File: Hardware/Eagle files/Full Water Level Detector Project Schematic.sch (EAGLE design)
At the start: 20 parts, among them IC1 74AHCT125, M1 SMALL_SERVO

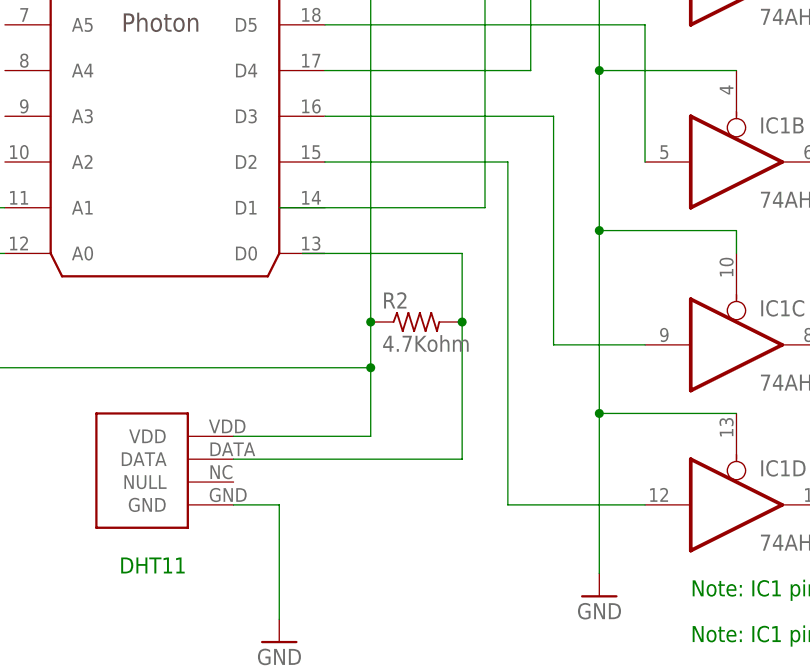
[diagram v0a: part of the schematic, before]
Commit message: Updated schematic
Changed DHT11 data to Photon D2 instead of D0.  D0 does not work with
Piettetech library.  Changed IC1D input to D0 to free up D2 for the
DHT11.
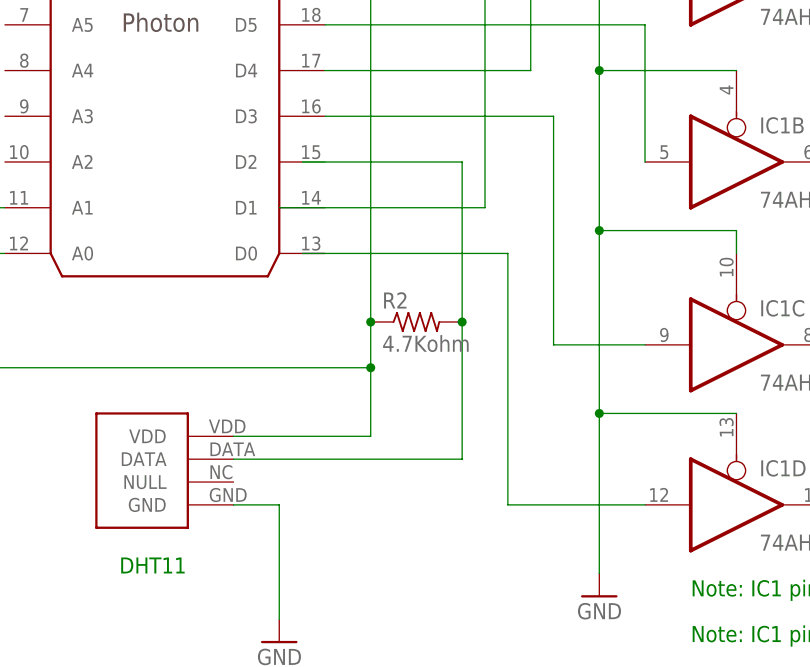
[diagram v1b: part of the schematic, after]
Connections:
- net N$17: no longer U$1G$1.D2
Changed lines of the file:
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@@
 <net name="N$17" class="0">
 <segment>
-<pinref part="U$1" gate="G$1" pin="D2"/>
-<wire x1="10.16" y1="48.26" x2="30.48" y2="48.26" width="0.1524" layer="91"/>
-<wire x1="30.48" y1="48.26" x2="30.48" y2="10.16" width="0.1524" layer="91"/>
 <pinref part="IC1" gate="D" pin="I"/>
 <wire x1="30.48" y1="10.16" x2="45.72" y2="10.16" width="0.1524" layer="91"/>
+<wire x1="7.62" y1="38.1" x2="30.48" y2="38.1" width="0.1524" layer="91"/>
+<wire x1="30.48" y1="38.1" x2="30.48" y2="10.16" width="0.1524" layer="91"/>
 </segment>
 </net>
@@
 <wire x1="0" y1="15.24" x2="25.4" y2="15.24" width="0.1524" layer="91"/>
 <wire x1="25.4" y1="15.24" x2="25.4" y2="30.48" width="0.1524" layer="91"/>
-<wire x1="25.4" y1="30.48" x2="25.4" y2="38.1" width="0.1524" layer="91"/>
-<wire x1="25.4" y1="38.1" x2="7.62" y2="38.1" width="0.1524" layer="91"/>
 <pinref part="R2" gate="G$1" pin="2"/>
+<wire x1="25.4" y1="30.48" x2="25.4" y2="48.26" width="0.1524" layer="91"/>
+<wire x1="25.4" y1="48.26" x2="7.62" y2="48.26" width="0.1524" layer="91"/>
 <junction x="25.4" y="30.48"/>
 </segment>

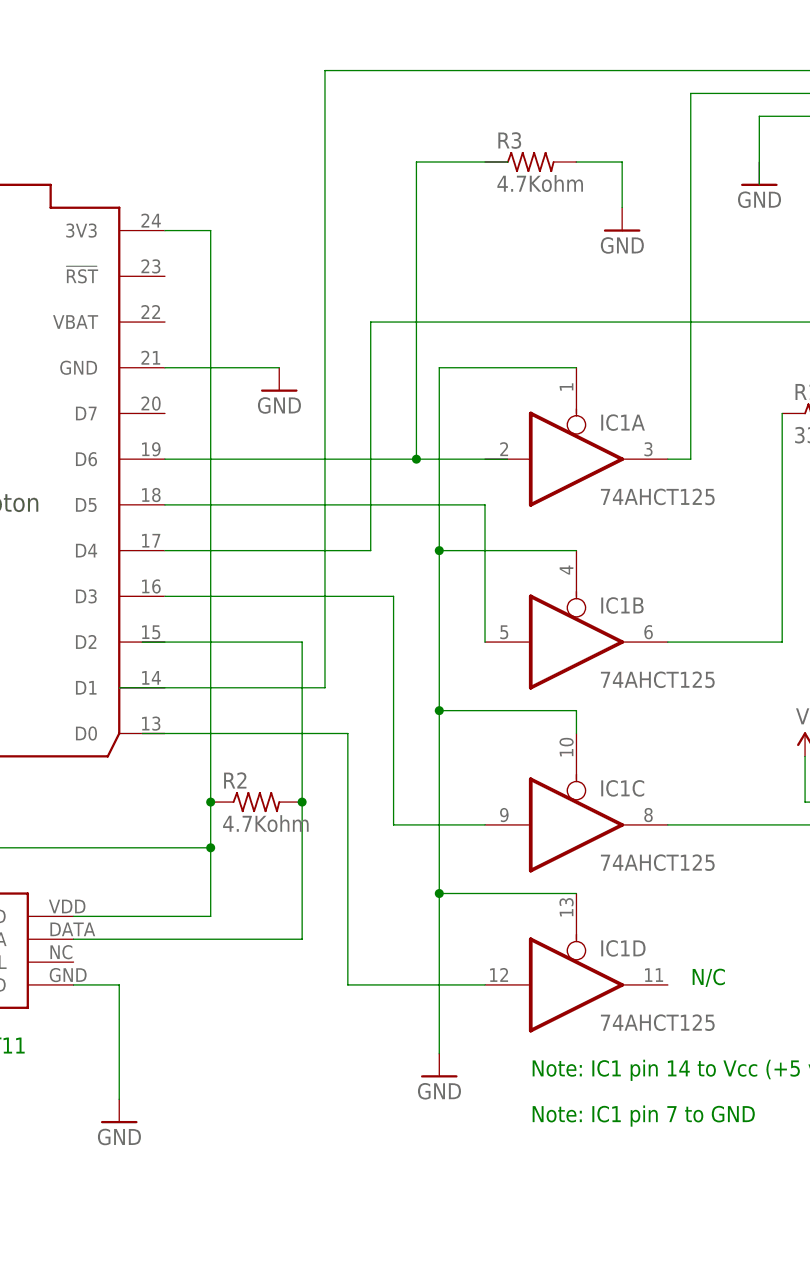
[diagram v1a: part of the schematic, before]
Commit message: Updated schematic
Placed 5.6 Kohm pulldown resistors on all input pins of the 74AHCT125 to
clamp off noise when the Photon is flashing/reset.  Used 5.6 Kohm in
lieu of 4.7 Kohm because that is what I had on hand.
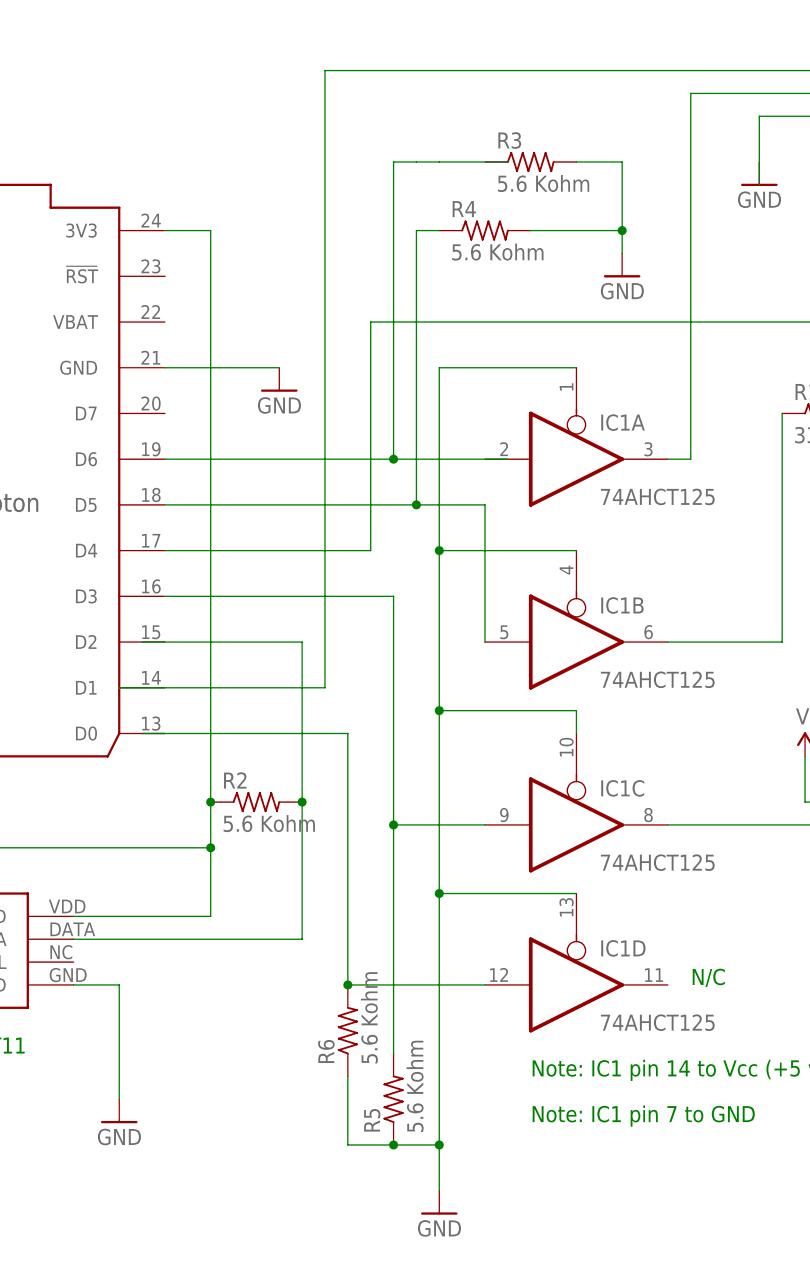
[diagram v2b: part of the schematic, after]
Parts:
- added R4, R5, R6: 5.6 Kohm, rcl:R-US_0309/12
- R2, R3: value 4.7Kohm -> 5.6 Kohm
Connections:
- net GND: now also R4.2, R5.1, R6.1
- net N$17: now also R6.2
- net N$6: now also R4.1
- net N$7: now also R5.2
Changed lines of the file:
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@@
 <part name="GND8" library="SparkFun-Aesthetics" deviceset="GND" device=""/>
 <part name="GND9" library="SparkFun-Aesthetics" deviceset="GND" device=""/>
-<part name="R2" library="rcl" deviceset="R-US_" device="0309/12" value="4.7Kohm"/>
+<part name="R2" library="rcl" deviceset="R-US_" device="0309/12" value="5.6 Kohm"/>
 <part name="TOGGLE" library="switch" deviceset="55?" device="01"/>
-<part name="R3" library="rcl" deviceset="R-US_" device="0309/12" value="4.7Kohm"/>
+<part name="R3" library="rcl" deviceset="R-US_" device="0309/12" value="5.6 Kohm"/>
 <part name="GND10" library="SparkFun-Aesthetics" deviceset="GND" device=""/>
+<part name="R4" library="rcl" deviceset="R-US_" device="0309/12" value="5.6 Kohm"/>
+<part name="R5" library="rcl" deviceset="R-US_" device="0309/12" value="5.6 Kohm"/>
+<part name="R6" library="rcl" deviceset="R-US_" device="0309/12" value="5.6 Kohm"/>
 </parts>
 <sheets>
@@
 <instance part="LED1" gate="G$1" x="119.38" y="73.66" rot="R90"/>
 <instance part="SP2" gate="G$1" x="111.76" y="104.14" rot="R270"/>
-<instance part="GND5" gate="1" x="40.64" y="0" rot="MR0"/>
+<instance part="GND5" gate="1" x="40.64" y="-15.24" rot="MR0"/>
 <instance part="U$2" gate="G$1" x="-15.24" y="7.62"/>
 <instance part="GND6" gate="1" x="5.08" y="-5.08" rot="MR0"/>
@@
 <instance part="TOGGLE" gate="G$1" x="106.68" y="129.54"/>
 <instance part="R3" gate="G$1" x="50.8" y="101.6"/>
-<instance part="GND10" gate="1" x="60.96" y="93.98" rot="MR0"/>
+<instance part="GND10" gate="1" x="60.96" y="88.9" rot="MR0"/>
+<instance part="R4" gate="G$1" x="45.72" y="93.98"/>
+<instance part="R5" gate="G$1" x="35.56" y="-2.54" rot="R90"/>
+<instance part="R6" gate="G$1" x="30.48" y="5.08" rot="R90"/>
 </instances>
 <busses>
@@
 <segment>
 <pinref part="GND5" gate="1" pin="GND"/>
-<wire x1="40.64" y1="2.54" x2="40.64" y2="20.32" width="0.1524" layer="91"/>
+<wire x1="40.64" y1="-12.7" x2="40.64" y2="-7.62" width="0.1524" layer="91"/>
 <pinref part="IC1" gate="A" pin="OE"/>
+<wire x1="40.64" y1="-7.62" x2="40.64" y2="20.32" width="0.1524" layer="91"/>
 <wire x1="40.64" y1="20.32" x2="40.64" y2="40.64" width="0.1524" layer="91"/>
 <wire x1="40.64" y1="40.64" x2="40.64" y2="58.42" width="0.1524" layer="91"/>
@@
 <junction x="40.64" y="40.64"/>
 <junction x="40.64" y="58.42"/>
+<pinref part="R5" gate="G$1" pin="1"/>
+<wire x1="35.56" y1="-7.62" x2="40.64" y2="-7.62" width="0.1524" layer="91"/>
+<junction x="40.64" y="-7.62"/>
+<pinref part="R6" gate="G$1" pin="1"/>
+<wire x1="30.48" y1="0" x2="30.48" y2="-7.62" width="0.1524" layer="91"/>
+<wire x1="30.48" y1="-7.62" x2="35.56" y2="-7.62" width="0.1524" layer="91"/>
+<junction x="35.56" y="-7.62"/>
 </segment>
 <segment>
@@
 <pinref part="GND10" gate="1" pin="GND"/>
 <wire x1="55.88" y1="101.6" x2="60.96" y2="101.6" width="0.1524" layer="91"/>
-<wire x1="60.96" y1="101.6" x2="60.96" y2="96.52" width="0.1524" layer="91"/>
+<wire x1="60.96" y1="101.6" x2="60.96" y2="93.98" width="0.1524" layer="91"/>
+<pinref part="R4" gate="G$1" pin="2"/>
+<wire x1="60.96" y1="93.98" x2="60.96" y2="91.44" width="0.1524" layer="91"/>
+<wire x1="50.8" y1="93.98" x2="60.96" y2="93.98" width="0.1524" layer="91"/>
+<junction x="60.96" y="93.98"/>
 </segment>
 </net>
@@
 <segment>
 <pinref part="U$1" gate="G$1" pin="D6"/>
-<wire x1="10.16" y1="68.58" x2="38.1" y2="68.58" width="0.1524" layer="91"/>
-<wire x1="38.1" y1="68.58" x2="48.26" y2="68.58" width="0.1524" layer="91"/>
-<wire x1="38.1" y1="68.58" x2="38.1" y2="101.6" width="0.1524" layer="91"/>
-<wire x1="38.1" y1="101.6" x2="48.26" y2="101.6" width="0.1524" layer="91"/>
-<junction x="38.1" y="68.58"/>
+<wire x1="10.16" y1="68.58" x2="35.56" y2="68.58" width="0.1524" layer="91"/>
+<wire x1="35.56" y1="68.58" x2="48.26" y2="68.58" width="0.1524" layer="91"/>
+<wire x1="35.56" y1="68.58" x2="35.56" y2="101.6" width="0.1524" layer="91"/>
+<wire x1="38.1" y1="101.6" x2="40.64" y2="101.6" width="0.1524" layer="91"/>
+<wire x1="40.64" y1="101.6" x2="48.26" y2="101.6" width="0.1524" layer="91"/>
+<wire x1="35.56" y1="101.6" x2="38.1" y2="101.6" width="0.1524" layer="91"/>
+<junction x="35.56" y="68.58"/>
 </segment>
 </net>
@@
 <segment>
 <pinref part="U$1" gate="G$1" pin="D5"/>
-<wire x1="10.16" y1="63.5" x2="45.72" y2="63.5" width="0.1524" layer="91"/>
+<wire x1="10.16" y1="63.5" x2="38.1" y2="63.5" width="0.1524" layer="91"/>
 <pinref part="IC1" gate="B" pin="I"/>
+<wire x1="38.1" y1="63.5" x2="45.72" y2="63.5" width="0.1524" layer="91"/>
 <wire x1="45.72" y1="63.5" x2="45.72" y2="48.26" width="0.1524" layer="91"/>
+<pinref part="R4" gate="G$1" pin="1"/>
+<wire x1="40.64" y1="93.98" x2="38.1" y2="93.98" width="0.1524" layer="91"/>
+<wire x1="38.1" y1="93.98" x2="38.1" y2="63.5" width="0.1524" layer="91"/>
+<junction x="38.1" y="63.5"/>
 </segment>
 </net>
@@
 <wire x1="35.56" y1="53.34" x2="35.56" y2="27.94" width="0.1524" layer="91"/>
 <wire x1="35.56" y1="27.94" x2="45.72" y2="27.94" width="0.1524" layer="91"/>
+<pinref part="R5" gate="G$1" pin="2"/>
+<wire x1="35.56" y1="2.54" x2="35.56" y2="27.94" width="0.1524" layer="91"/>
+<junction x="35.56" y="27.94"/>
 </segment>
 </net>
@@
 <wire x1="7.62" y1="38.1" x2="30.48" y2="38.1" width="0.1524" layer="91"/>
 <wire x1="30.48" y1="38.1" x2="30.48" y2="10.16" width="0.1524" layer="91"/>
-</segment>
-</net>
+<pinref part="R6" gate="G$1" pin="2"/>
+<junction x="30.48" y="10.16"/>
+</segment>
+</net>

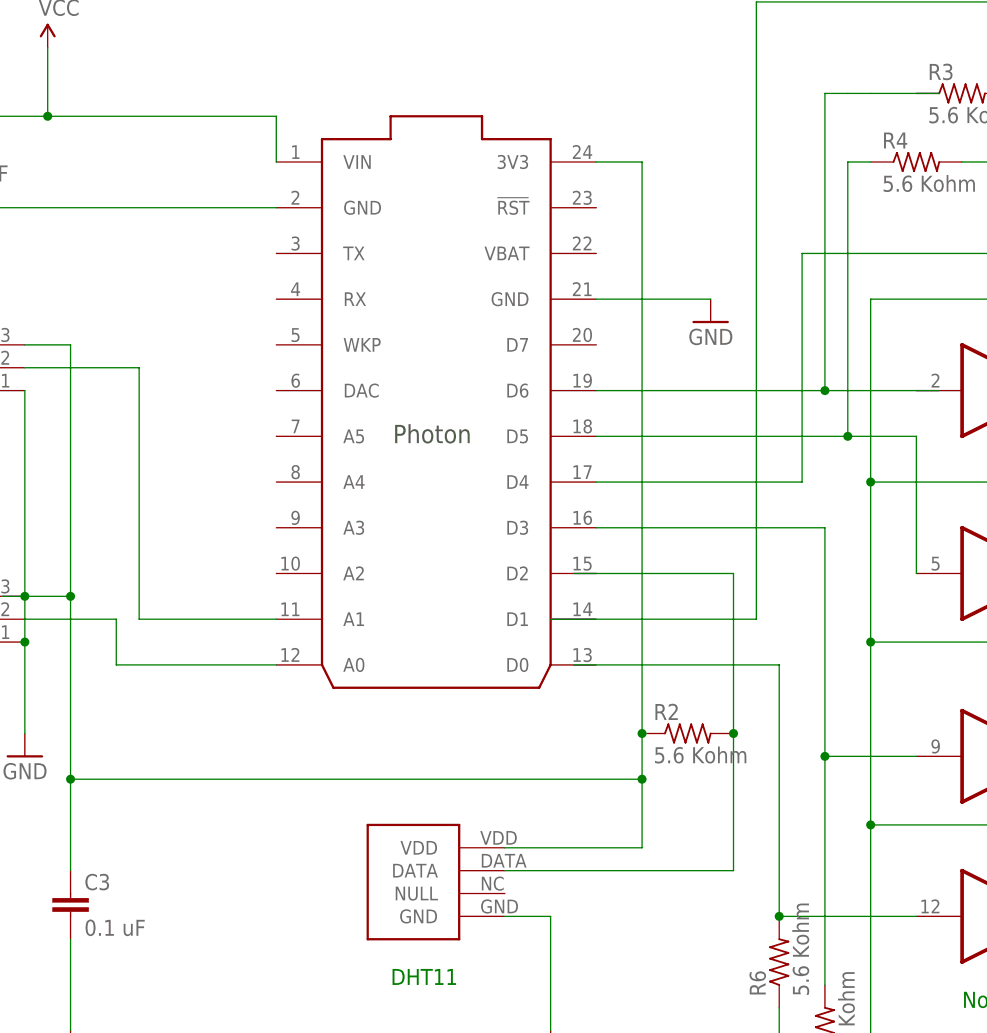
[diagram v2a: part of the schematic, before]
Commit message: Changed servo control pin to A5
Changed the servo control pin from D3 to A5 for compatibility with Core,
Photon and Electron (according to Particle documentation).
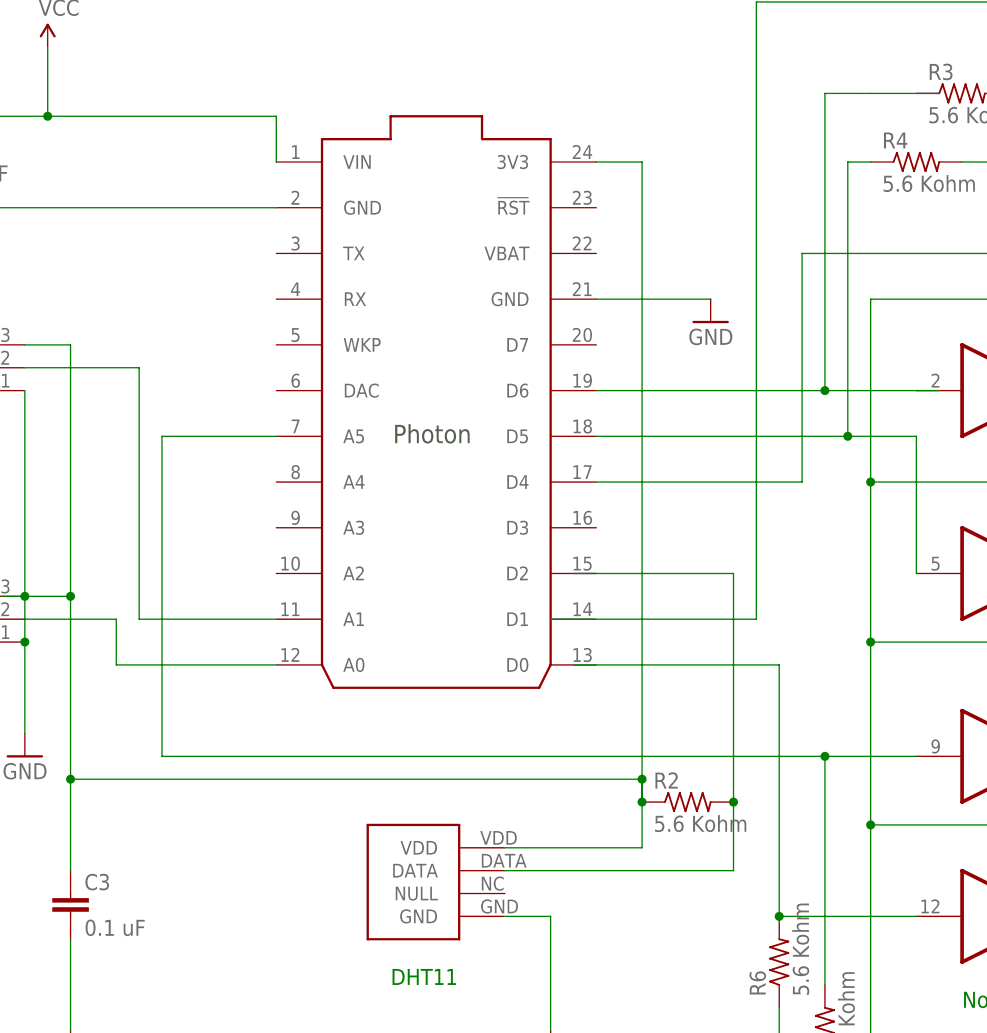
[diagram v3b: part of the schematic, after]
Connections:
- net N$7: now also U$1G$1.A5; no longer U$1G$1.D3
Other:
- moved on the sheet: R2
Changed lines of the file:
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@@
 <instance part="GND8" gate="1" x="93.98" y="55.88" rot="MR0"/>
 <instance part="GND9" gate="1" x="22.86" y="76.2" rot="MR0"/>
-<instance part="R2" gate="G$1" x="20.32" y="30.48"/>
+<instance part="R2" gate="G$1" x="20.32" y="22.86"/>
 <instance part="TOGGLE" gate="G$1" x="106.68" y="129.54"/>
 <instance part="R3" gate="G$1" x="50.8" y="101.6"/>
@@
 <segment>
 <pinref part="IC1" gate="C" pin="I"/>
-<pinref part="U$1" gate="G$1" pin="D3"/>
-<wire x1="10.16" y1="53.34" x2="35.56" y2="53.34" width="0.1524" layer="91"/>
-<wire x1="35.56" y1="53.34" x2="35.56" y2="27.94" width="0.1524" layer="91"/>
 <wire x1="35.56" y1="27.94" x2="45.72" y2="27.94" width="0.1524" layer="91"/>
 <pinref part="R5" gate="G$1" pin="2"/>
 <wire x1="35.56" y1="2.54" x2="35.56" y2="27.94" width="0.1524" layer="91"/>
+<wire x1="35.56" y1="27.94" x2="-38.1" y2="27.94" width="0.1524" layer="91"/>
+<wire x1="-38.1" y1="27.94" x2="-38.1" y2="63.5" width="0.1524" layer="91"/>
+<pinref part="U$1" gate="G$1" pin="A5"/>
+<wire x1="-38.1" y1="63.5" x2="-25.4" y2="63.5" width="0.1524" layer="91"/>
 <junction x="35.56" y="27.94"/>
 </segment>
@@
 <pinref part="U$1" gate="G$1" pin="3V3"/>
 <wire x1="10.16" y1="93.98" x2="15.24" y2="93.98" width="0.1524" layer="91"/>
-<wire x1="15.24" y1="93.98" x2="15.24" y2="30.48" width="0.1524" layer="91"/>
+<wire x1="15.24" y1="93.98" x2="15.24" y2="22.86" width="0.1524" layer="91"/>
 <pinref part="U$2" gate="G$1" pin="VDD"/>
-<wire x1="15.24" y1="30.48" x2="15.24" y2="25.4" width="0.1524" layer="91"/>
+<wire x1="15.24" y1="22.86" x2="15.24" y2="25.4" width="0.1524" layer="91"/>
 <wire x1="15.24" y1="25.4" x2="15.24" y2="17.78" width="0.1524" layer="91"/>
 <wire x1="15.24" y1="17.78" x2="0" y2="17.78" width="0.1524" layer="91"/>
@@
 <junction x="15.24" y="25.4"/>
 <pinref part="R2" gate="G$1" pin="1"/>
-<junction x="15.24" y="30.48"/>
+<junction x="15.24" y="22.86"/>
 </segment>
 </net>
@@
 <pinref part="U$2" gate="G$1" pin="DATA"/>
 <wire x1="0" y1="15.24" x2="25.4" y2="15.24" width="0.1524" layer="91"/>
-<wire x1="25.4" y1="15.24" x2="25.4" y2="30.48" width="0.1524" layer="91"/>
+<wire x1="25.4" y1="15.24" x2="25.4" y2="22.86" width="0.1524" layer="91"/>
 <pinref part="R2" gate="G$1" pin="2"/>
-<wire x1="25.4" y1="30.48" x2="25.4" y2="48.26" width="0.1524" layer="91"/>
+<wire x1="25.4" y1="22.86" x2="25.4" y2="48.26" width="0.1524" layer="91"/>
 <wire x1="25.4" y1="48.26" x2="7.62" y2="48.26" width="0.1524" layer="91"/>
-<junction x="25.4" y="30.48"/>
-</segment>
-</net>
+<junction x="25.4" y="22.86"/>
+</segment>
+</net>
